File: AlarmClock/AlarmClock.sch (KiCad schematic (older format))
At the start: 7 parts

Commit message: Added op amp circuit
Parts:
- removed R?: RES, symbol RES
- added C2: 250uF, symbol CAP_POL
- added LS?: Speaker, symbol Speaker
- C1: renamed from C?; value CAP -> 0.05uF
- C3: renamed from C?; value CAP -> Opt
- POT1: renamed from RV?; value POT -> 10K
- R1: renamed from R?; value RES -> 10
- R2: renamed from R?; value RES -> Opt
- gave numbers to parts that had none: 1
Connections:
- wire segments 9 -> 18
- no-connect marks 0 -> 1
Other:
- moved on the sheet: C1, C3, R1, R2
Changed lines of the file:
@@
 LIBS:contrib
 LIBS:valves
+LIBS:AlarmClock-cache
 EELAYER 25 0
 EELAYER END
@@
 $EndDescr
 $Comp
-L LM386 U?
+L LM386 U1
 U 1 1 5B2324A3
 P 2050 1900
-F 0 "U?" H 2100 2200 50  0000 L CNN
+F 0 "U1" H 2100 2200 50  0000 L CNN
 F 1 "LM386" H 2100 2100 50  0000 L CNN
 F 2 "" H 2150 2000 50  0001 C CNN
@@
 $EndComp
 $Comp
-L RES R?
+L RES R2
 U 1 1 5B23262B
-P 850 1000
-F 0 "R?" H 850 1175 40  0000 C CNN
-F 1 "RES" H 850 1100 40  0000 C CNN
-F 2 "" H 850 1070 30  0000 C CNN
-F 3 "" V 850 1000 30  0000 C CNN
-	1    850  1000
-	1    0    0    -1
-$EndComp
-$Comp
-L RES R?
+P 2500 1150
+F 0 "R2" H 2500 1325 40  0000 C CNN
+F 1 "Opt" H 2500 1250 40  0000 C CNN
+F 2 "" H 2500 1220 30  0000 C CNN
+F 3 "" V 2500 1150 30  0000 C CNN
+	1    2500 1150
+	1    0    0    -1
+$EndComp
+$Comp
+L RES R1
 U 1 1 5B232694
-P 850 1250
-F 0 "R?" H 850 1425 40  0000 C CNN
-F 1 "RES" H 850 1350 40  0000 C CNN
-F 2 "" H 850 1320 30  0000 C CNN
-F 3 "" V 850 1250 30  0000 C CNN
-	1    850  1250
-	1    0    0    -1
-$EndComp
-$Comp
-L RES R?
-U 1 1 5B2326F5
-P 850 1450
-F 0 "R?" H 850 1625 40  0000 C CNN
-F 1 "RES" H 850 1550 40  0000 C CNN
-F 2 "" H 850 1520 30  0000 C CNN
-F 3 "" V 850 1450 30  0000 C CNN
-	1    850  1450
-	1    0    0    -1
-$EndComp
-$Comp
-L POT RV?
+P 2600 2600
+F 0 "R1" H 2600 2775 40  0000 C CNN
+F 1 "10" H 2600 2700 40  0000 C CNN
+F 2 "" H 2600 2670 30  0000 C CNN
+F 3 "" V 2600 2600 30  0000 C CNN
+	1    2600 2600
+	0    1    1    0
+$EndComp
+$Comp
+L POT POT1
 U 1 1 5B2327B4
 P 1400 2000
-F 0 "RV?" V 1225 2000 50  0000 C CNN
-F 1 "POT" V 1300 2000 50  0000 C CNN
+F 0 "POT1" V 1225 2000 50  0000 C CNN
+F 1 "10K" V 1300 2000 50  0000 C CNN
 F 2 "" H 1400 2000 50  0001 C CNN
 F 3 "" H 1400 2000 50  0001 C CNN
@@
 $EndComp
 $Comp
-L CAP C?
+L CAP C1
 U 1 1 5B23285D
-P 1250 750
-F 0 "C?" H 1250 975 40  0000 C CNN
-F 1 "CAP" H 1250 900 40  0000 C CNN
-F 2 "" H 1250 820 30  0000 C CNN
-F 3 "" V 1250 750 30  0000 C CNN
-	1    1250 750
-	1    0    0    -1
-$EndComp
-$Comp
-L CAP C?
+P 2600 2200
+F 0 "C1" H 2600 2425 40  0000 C CNN
+F 1 "0.05uF" H 2600 2350 40  0000 C CNN
+F 2 "" H 2600 2270 30  0000 C CNN
+F 3 "" V 2600 2200 30  0000 C CNN
+	1    2600 2200
+	0    1    -1   0
+$EndComp
+$Comp
+L CAP C3
 U 1 1 5B2328BE
-P 2100 950
-F 0 "C?" H 2100 1175 40  0000 C CNN
-F 1 "CAP" H 2100 1100 40  0000 C CNN
-F 2 "" H 2100 1020 30  0000 C CNN
-F 3 "" V 2100 950 30  0000 C CNN
-	1    2100 950
+P 2900 1150
+F 0 "C3" H 2900 1375 40  0000 C CNN
+F 1 "Opt" H 2900 1300 40  0000 C CNN
+F 2 "" H 2900 1220 30  0000 C CNN
+F 3 "" V 2900 1150 30  0000 C CNN
+	1    2900 1150
 	1    0    0    -1
 $EndComp
@@
 	1    0    0    1
 $EndComp
+NoConn ~ 2050 2200
+Wire Wire Line
+	2050 1600 2050 1150
+Wire Wire Line
+	2050 1150 2250 1150
+Wire Wire Line
+	3050 1150 3050 1600
+Wire Wire Line
+	3050 1600 2150 1600
+Wire Wire Line
+	2350 1900 3050 1900
+Wire Wire Line
+	2600 1900 2600 2050
+$Comp
+L GND #PWR?
+U 1 1 5B232F3C
+P 2600 2850
+F 0 "#PWR?" H 2600 2600 50  0001 C CNN
+F 1 "GND" H 2600 2700 50  0000 C CNN
+F 2 "" H 2600 2850 50  0001 C CNN
+F 3 "" H 2600 2850 50  0001 C CNN
+	1    2600 2850
+	1    0    0    -1
+$EndComp
+Connection ~ 2600 1900
+Wire Wire Line
+	3350 1900 3700 1900
+Wire Wire Line
+	3700 1900 3700 2250
+$Comp
+L CAP_POL C2
+U 1 1 5B2331BA
+P 3200 1900
+F 0 "C2" H 3200 2125 40  0000 C CNN
+F 1 "250uF" H 3200 2050 40  0000 C CNN
+F 2 "" H 3200 1970 30  0000 C CNN
+F 3 "" V 3200 1900 30  0000 C CNN
+	1    3200 1900
+	1    0    0    -1
+$EndComp
+$Comp
+L Speaker LS?
+U 1 1 5B2332D9
+P 3900 2250
+F 0 "LS?" H 3950 2475 50  0000 R CNN
+F 1 "Speaker" H 3950 2400 50  0000 R CNN
+F 2 "" H 3900 2050 50  0001 C CNN
+F 3 "" H 3890 2200 50  0001 C CNN
+	1    3900 2250
+	1    0    0    -1
+$EndComp
+Wire Wire Line
+	3700 2350 3700 2700
+$Comp
+L GND #PWR?
+U 1 1 5B23335D
+P 3700 2700
+F 0 "#PWR?" H 3700 2450 50  0001 C CNN
+F 1 "GND" H 3700 2550 50  0000 C CNN
+F 2 "" H 3700 2700 50  0001 C CNN
+F 3 "" H 3700 2700 50  0001 C CNN
+	1    3700 2700
+	1    0    0    -1
+$EndComp
 $EndSCHEMATC

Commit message: STM Board added to op amp schematic
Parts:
- added STM?: STM32_F4, symbol STM32_F4
- gave numbers to parts that had none: 1
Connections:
- net labels added: PA4, PC11, PC4, PC5, PC8, PC9, PD10, PD11, PD4, PD7, PD8, PD9, PE10, PE11, PE12, PE13, PE14, PE15, PE6, PE7, PE8, PE9
- net labels removed: Vin
- wire segments 18 -> 43
- no-connect marks 1 -> 62
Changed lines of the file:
@@
 	1400 1850 850  1850
 Text GLabel 850  1850 0    60   Input ~ 0
-Vin
+PA4
 Wire Wire Line
 	1800 1800 1750 1800
@@
 $EndComp
 $Comp
-L Speaker LS?
+L Speaker LS1
 U 1 1 5B2332D9
 P 3900 2250
-F 0 "LS?" H 3950 2475 50  0000 R CNN
+F 0 "LS1" H 3950 2475 50  0000 R CNN
 F 1 "Speaker" H 3950 2400 50  0000 R CNN
 F 2 "" H 3900 2050 50  0001 C CNN
@@
 	1    0    0    -1
 $EndComp
+$Comp
+L STM32_F4 STM?
+U 1 1 5B2807A9
+P 5900 3750
+F 0 "STM?" H 5900 3850 60  0000 C CNN
+F 1 "STM32_F4" H 5900 3650 60  0000 C CNN
+F 2 "" H 5900 3750 60  0000 C CNN
+F 3 "" H 5900 3750 60  0000 C CNN
+	1    5900 3750
+	1    0    0    -1
+$EndComp
+Text GLabel 4650 5200 0    60   Input ~ 0
+PA4
+Wire Wire Line
+	4900 5200 4650 5200
+Wire Wire Line
+	4550 1800 4900 1800
+Text GLabel 4550 1800 0    60   Input ~ 0
+PC4
+Text GLabel 4550 1900 0    60   Input ~ 0
+PC5
+Wire Wire Line
+	4550 1900 4900 1900
+Text GLabel 4550 2200 0    60   Input ~ 0
+PC8
+Text GLabel 4550 2300 0    60   Input ~ 0
+PC9
+Text GLabel 4550 2500 0    60   Input ~ 0
+PC11
+Wire Wire Line
+	4550 2200 4900 2200
+Wire Wire Line
+	4550 2300 4900 2300
+Wire Wire Line
+	4550 2500 4900 2500
+Text GLabel 7250 1800 2    60   Input ~ 0
+PD4
+Text GLabel 7250 2100 2    60   Input ~ 0
+PD7
+Wire Wire Line
+	6900 5800 6900 6250
+Wire Wire Line
+	5200 6450 6350 6450
+Wire Wire Line
+	5200 6450 5200 6500
+$Comp
+L GND #PWR?
+U 1 1 5B28351C
+P 5200 6500
+F 0 "#PWR?" H 5200 6250 50  0001 C CNN
+F 1 "GND" H 5200 6350 50  0000 C CNN
+F 2 "" H 5200 6500 50  0001 C CNN
+F 3 "" H 5200 6500 50  0001 C CNN
+	1    5200 6500
+	1    0    0    -1
+$EndComp
+$Comp
+L GND #PWR?
+U 1 1 5B283542
+P 6900 6250
+F 0 "#PWR?" H 6900 6000 50  0001 C CNN
+F 1 "GND" H 6900 6100 50  0000 C CNN
+F 2 "" H 6900 6250 50  0001 C CNN
+F 3 "" H 6900 6250 50  0001 C CNN
+	1    6900 6250
+	1    0    0    -1
+$EndComp
+Connection ~ 5450 6450
+Connection ~ 5550 6450
+Connection ~ 5650 6450
+Connection ~ 5750 6450
+Connection ~ 5850 6450
+Connection ~ 5950 6450
+Connection ~ 6050 6450
+Connection ~ 6150 6450
+Connection ~ 6250 6450
+Connection ~ 6900 6100
+Connection ~ 6900 6000
+Connection ~ 6900 5900
+Text GLabel 7250 2200 2    60   Input ~ 0
+PD8
+Text GLabel 7250 2300 2    60   Input ~ 0
+PD9
+Text GLabel 7250 2400 2    60   Input ~ 0
+PD10
+Text GLabel 7250 2500 2    60   Input ~ 0
+PD11
+Wire Wire Line
+	7250 1800 6900 1800
+Wire Wire Line
+	7250 2100 6900 2100
+Wire Wire Line
+	7250 2200 6900 2200
+Wire Wire Line
+	7250 2300 6900 2300
+Wire Wire Line
+	7250 2400 6900 2400
+Wire Wire Line
+	7250 2500 6900 2500
+Text GLabel 7300 3700 2    60   Input ~ 0
+PE6
+Text GLabel 7300 3800 2    60   Input ~ 0
+PE7
+Text GLabel 7300 3900 2    60   Input ~ 0
+PE8
+Text GLabel 7300 4000 2    60   Input ~ 0
+PE9
+Text GLabel 7300 4100 2    60   Input ~ 0
+PE10
+Text GLabel 7300 4200 2    60   Input ~ 0
+PE11
+Text GLabel 7300 4300 2    60   Input ~ 0
+PE12
+Text GLabel 7300 4400 2    60   Input ~ 0
+PE13
+Text GLabel 7300 4500 2    60   Input ~ 0
+PE14
+Text GLabel 7300 4600 2    60   Input ~ 0
+PE15
+Wire Wire Line
+	7300 3700 6900 3700
+Wire Wire Line
+	7300 3800 6900 3800
+Wire Wire Line
+	7300 3900 6900 3900
+Wire Wire Line
+	7300 4000 6900 4000
+Wire Wire Line
+	7300 4100 6900 4100
+Wire Wire Line
+	7300 4200 6900 4200
+Wire Wire Line
+	6900 4300 7300 4300
+Wire Wire Line
+	7300 4400 6900 4400
+Wire Wire Line
+	6900 4500 7300 4500
+Wire Wire Line
+	7300 4600 6900 4600
+NoConn ~ 4900 2600
+NoConn ~ 4900 2700
+NoConn ~ 4900 2800
+NoConn ~ 4900 2900
+NoConn ~ 4900 3100
+NoConn ~ 4900 3200
+NoConn ~ 4900 3300
+NoConn ~ 4900 3400
+NoConn ~ 4900 3500
+NoConn ~ 4900 3600
+NoConn ~ 4900 3700
+NoConn ~ 4900 3800
+NoConn ~ 4900 3900
+NoConn ~ 4900 4000
+NoConn ~ 4900 4100
+NoConn ~ 4900 4200
+NoConn ~ 4900 4300
+NoConn ~ 4900 4400
+NoConn ~ 4900 4500
+NoConn ~ 4900 4600
+NoConn ~ 4900 4800
+NoConn ~ 4900 4900
+NoConn ~ 4900 5000
+NoConn ~ 4900 5100
+NoConn ~ 4900 5300
+NoConn ~ 4900 5400
+NoConn ~ 4900 5500
+NoConn ~ 4900 5600
+NoConn ~ 4900 5700
+NoConn ~ 4900 5800
+NoConn ~ 4900 5900
+NoConn ~ 4900 6000
+NoConn ~ 4900 6100
+NoConn ~ 6900 5550
+NoConn ~ 6900 5350
+NoConn ~ 6900 5150
+NoConn ~ 6900 5050
+NoConn ~ 6900 4850
+NoConn ~ 6900 3600
+NoConn ~ 6900 3500
+NoConn ~ 6900 3400
+NoConn ~ 6900 3300
+NoConn ~ 6900 3200
+NoConn ~ 6900 3100
+NoConn ~ 6900 2900
+NoConn ~ 6900 2800
+NoConn ~ 6900 2700
+NoConn ~ 6900 2600
+NoConn ~ 4900 2400
+NoConn ~ 4900 2100
+NoConn ~ 4900 2000
+NoConn ~ 6900 2000
+NoConn ~ 6900 1900
+NoConn ~ 6900 1700
+NoConn ~ 6900 1600
+NoConn ~ 6900 1500
+NoConn ~ 6900 1400
+NoConn ~ 4900 1700
+NoConn ~ 4900 1600
+NoConn ~ 4900 1500
+NoConn ~ 4900 1400
 $EndSCHEMATC

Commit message: added labels to STM
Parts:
- C3, R2: value Opt -> 0
- STM1: renamed from STM?; value STM32_F4 -> STM32_F407
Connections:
- net labels removed: VCC
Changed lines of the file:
@@
 P 2500 1150
 F 0 "R2" H 2500 1325 40  0000 C CNN
-F 1 "Opt" H 2500 1250 40  0000 C CNN
+F 1 "0" H 2500 1250 40  0000 C CNN
 F 2 "" H 2500 1220 30  0000 C CNN
 F 3 "" V 2500 1150 30  0000 C CNN
@@
 P 2900 1150
 F 0 "C3" H 2900 1375 40  0000 C CNN
-F 1 "Opt" H 2900 1300 40  0000 C CNN
+F 1 "0" H 2900 1300 40  0000 C CNN
 F 2 "" H 2900 1220 30  0000 C CNN
 F 3 "" V 2900 1150 30  0000 C CNN
@@
 	1    1600 1350
 	1    0    0    -1
-$EndComp
-$Comp
-L VCC #PWR?
-U 1 1 5B233032
-P 1950 2200
-F 0 "#PWR?" H 1950 2050 50  0001 C CNN
-F 1 "VCC" H 1950 2350 50  0000 C CNN
-F 2 "" H 1950 2200 50  0001 C CNN
-F 3 "" H 1950 2200 50  0001 C CNN
-	1    1950 2200
-	1    0    0    1
 $EndComp
 NoConn ~ 2050 2200
@@
 $EndComp
 $Comp
-L STM32_F4 STM?
+L STM32_F4 STM1
 U 1 1 5B2807A9
 P 5900 3750
-F 0 "STM?" H 5900 3850 60  0000 C CNN
-F 1 "STM32_F4" H 5900 3650 60  0000 C CNN
+F 0 "STM1" H 5900 3850 60  0000 C CNN
+F 1 "STM32_F407" H 5900 3650 60  0000 C CNN
 F 2 "" H 5900 3750 60  0000 C CNN
 F 3 "" H 5900 3750 60  0000 C CNN

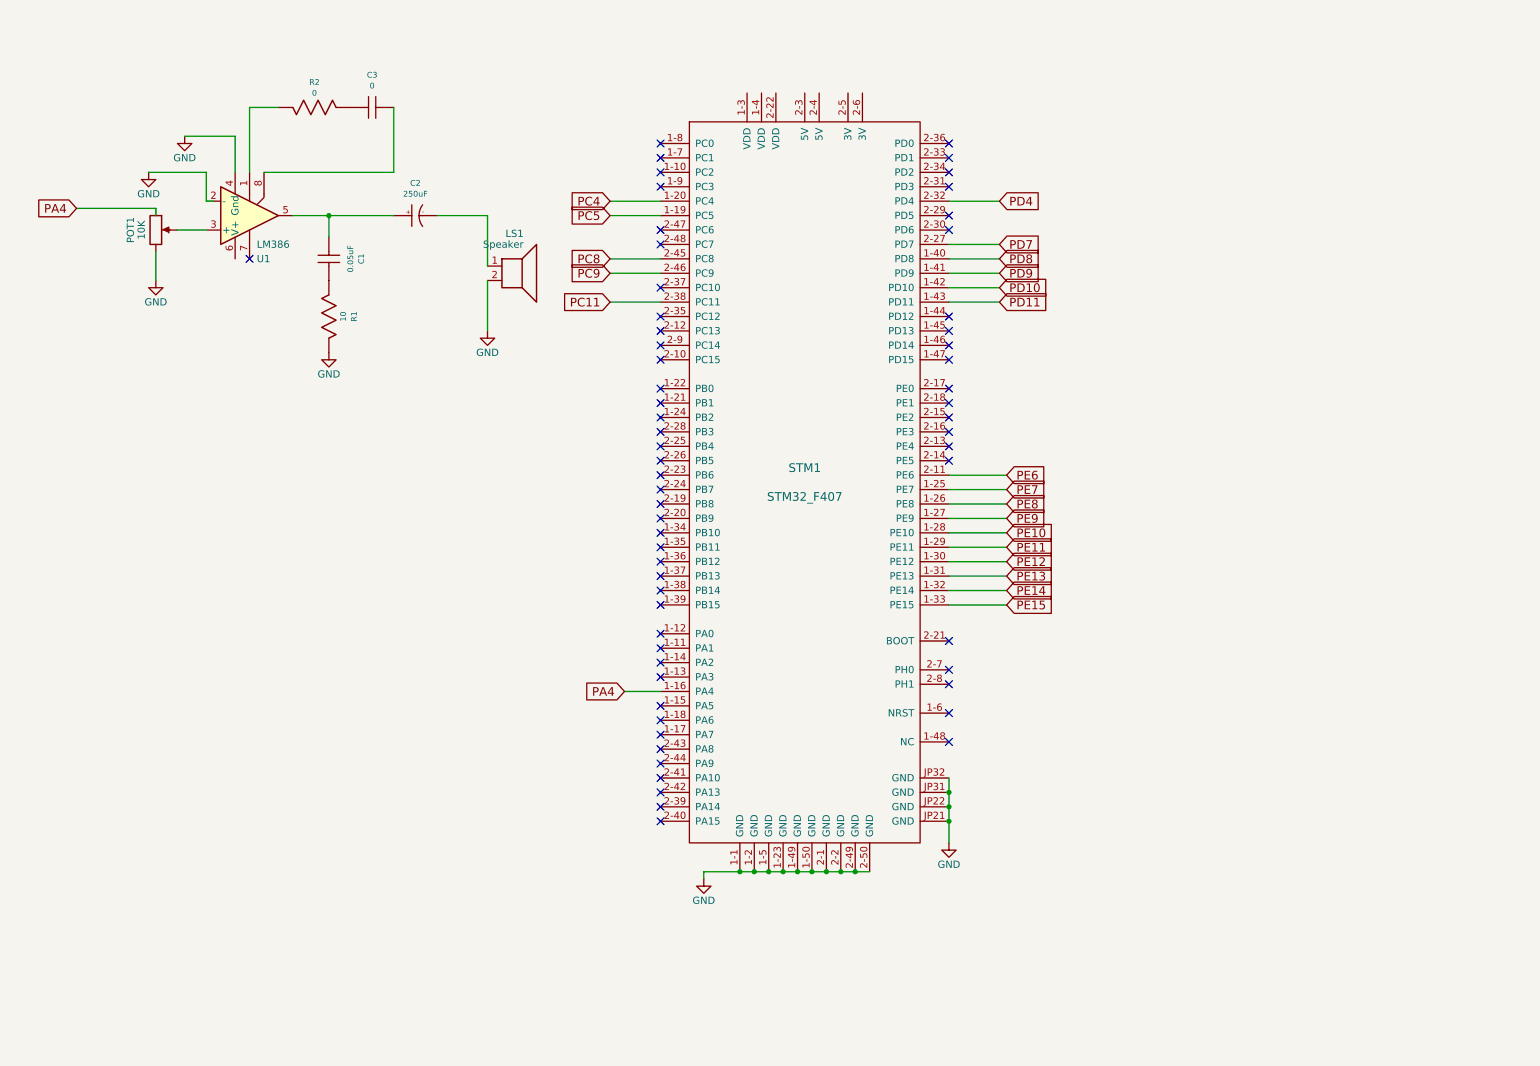
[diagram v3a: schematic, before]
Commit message: push button circuit added
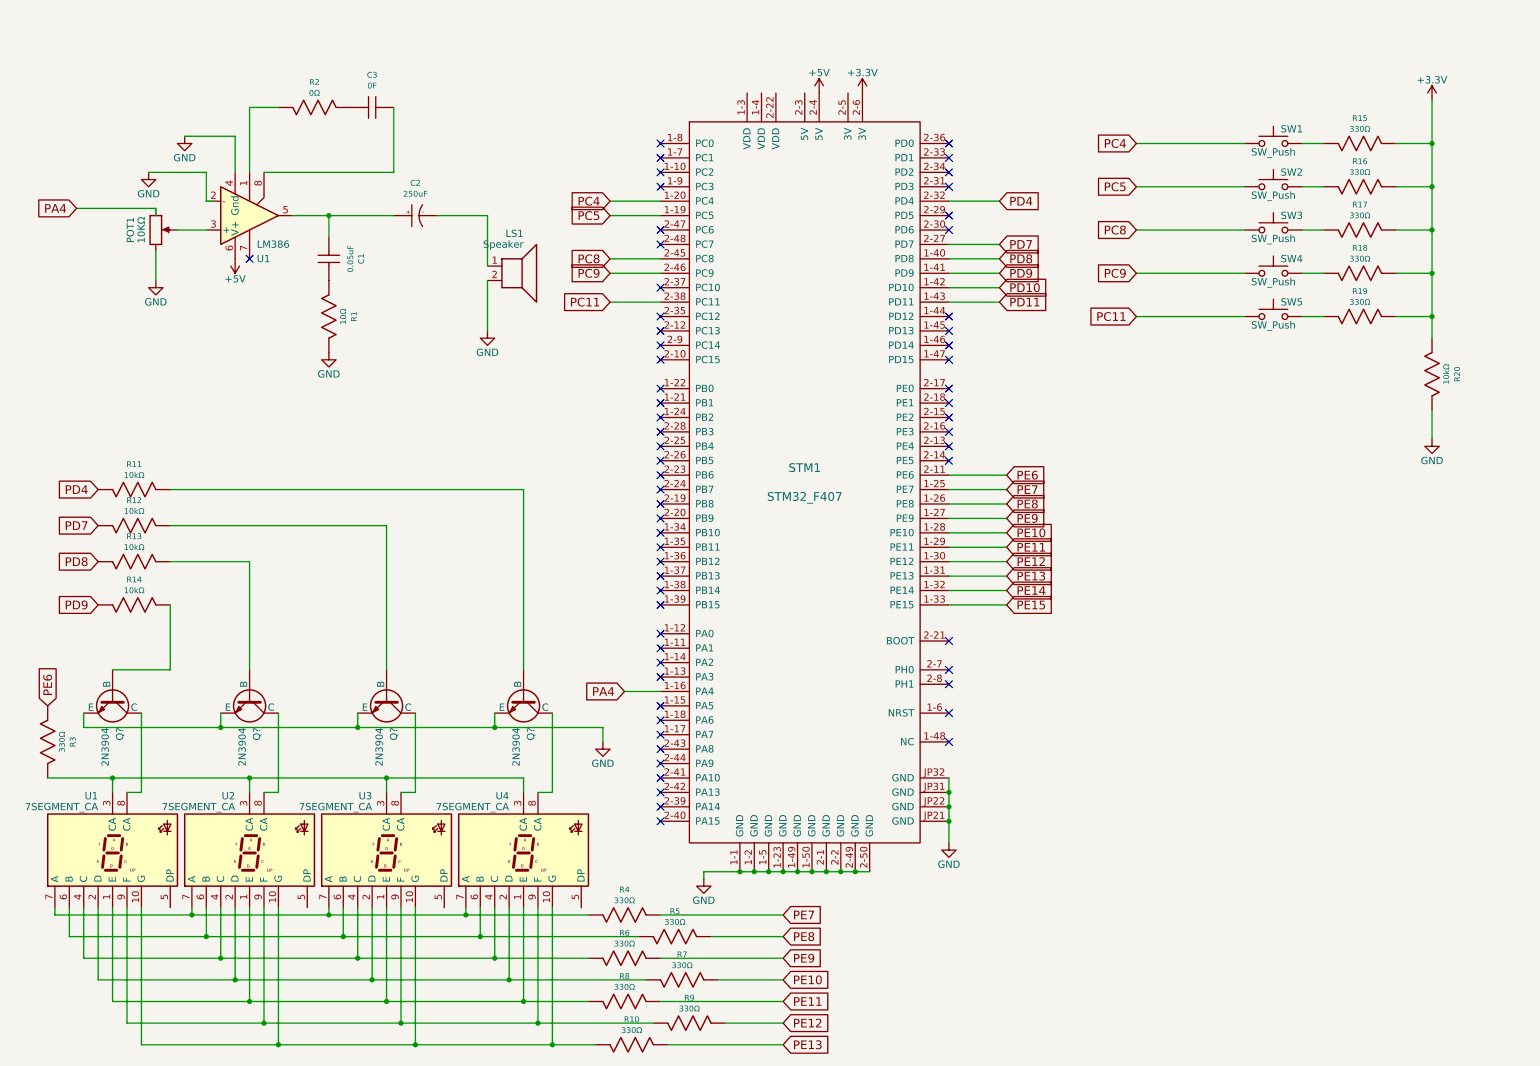
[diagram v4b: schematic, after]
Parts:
- added Q? (x4): 2N3904, symbol 2N3904
- added R10, R15, R16, R17, R18, R19, R3, R4, R5, R6, R7, R8, R9: 330Ω, symbol RES
- added R11, R12, R13, R14, R20: 10kΩ, symbol RES
- added SW1, SW2, SW3, SW4, SW5: SW_Push, symbol SW_Push
- added U1, U2, U3, U4: 7SEGMENT_CA, symbol 7SEGMENT_CA
- C3: value 0 -> 0F
- POT1: value 10K -> 10KΩ
- R1: value 10 -> 10Ω
- R2: value 0 -> 0Ω
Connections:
- net labels added: +3.3V, +5V
- wire segments 43 -> 129
